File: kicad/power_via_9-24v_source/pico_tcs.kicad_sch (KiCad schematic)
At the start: 14 parts, among them J1 TCS/Power, J2 Conn_01x20_Male, J3 Conn_01x20_Male, J4 Keypad, J5 Display, U1 L7805, U2 ULN2003

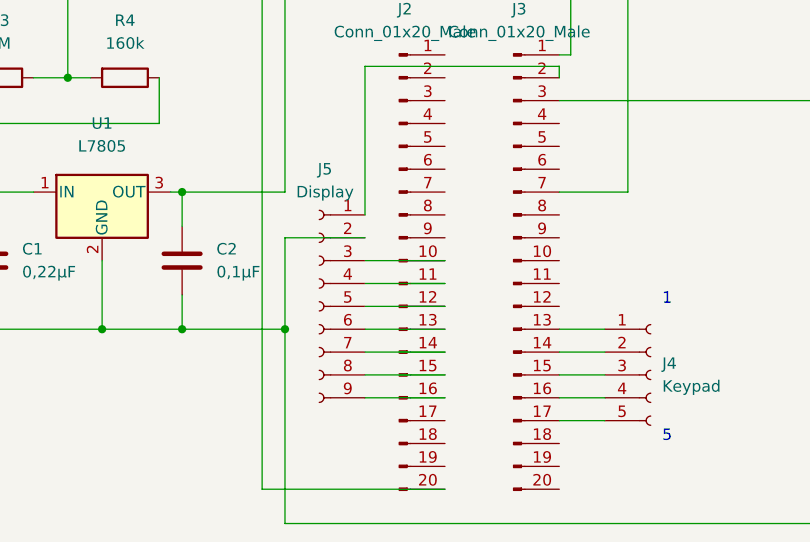
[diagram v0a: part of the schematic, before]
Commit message: fixed bug in connection between display and pico
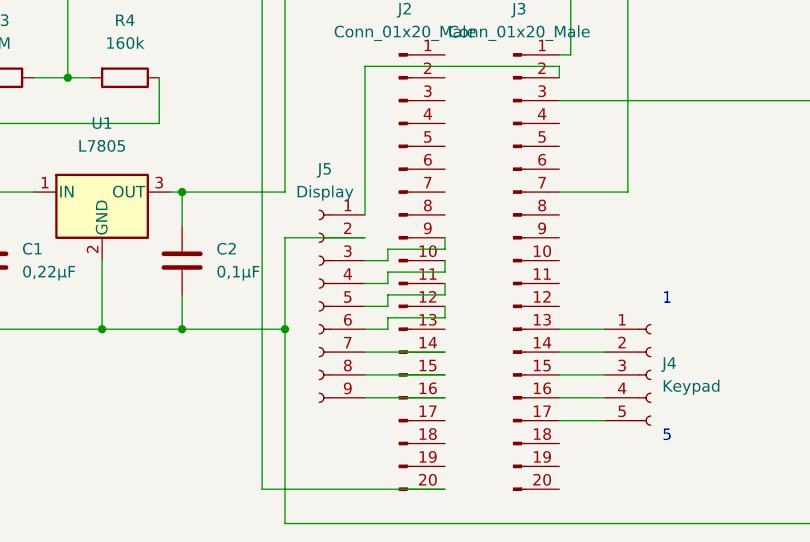
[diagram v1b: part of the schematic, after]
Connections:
- net at J5.3 (Pin_3): now also J2.9 (Pin_9); no longer J2.10 (Pin_10)
- net at J5.4 (Pin_4): now also J2.10 (Pin_10); no longer J2.11 (Pin_11)
- net at J5.5 (Pin_5): now also J2.11 (Pin_11); no longer J2.12 (Pin_12)
- net at J5.6 (Pin_6): now also J2.12 (Pin_12); no longer J2.13 (Pin_13)
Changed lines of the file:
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@@
+    (stroke (width 0) (type default) (color 0 0 0 0))
+  )
+  (wire (pts (xy 121.92 68.58) (xy 128.27 68.58))
     (stroke (width 0) (type default) (color 0 0 0 0))
   )
@@
     (stroke (width 0) (type default) (color 0 0 0 0))
   )
+  (wire (pts (xy 119.38 67.31) (xy 121.92 67.31))
+    (stroke (width 0) (type default) (color 0 0 0 0))
+  )
+  (wire (pts (xy 121.92 64.77) (xy 121.92 63.5))
+    (stroke (width 0) (type default) (color 0 0 0 0))
+  )
   (wire (pts (xy 119.38 59.69) (xy 110.49 59.69))
     (stroke (width 0) (type default) (color 0 0 0 0))
@@
     (stroke (width 0) (type default) (color 0 0 0 0))
   )
+  (wire (pts (xy 128.27 63.5) (xy 128.27 62.23))
+    (stroke (width 0) (type default) (color 0 0 0 0))
+  )
+  (wire (pts (xy 121.92 66.04) (xy 128.27 66.04))
+    (stroke (width 0) (type default) (color 0 0 0 0))
+  )
   (wire (pts (xy 110.49 69.85) (xy 99.06 69.85))
     (stroke (width 0) (type default) (color 0 0 0 0))
   )
-  (wire (pts (xy 119.38 69.85) (xy 128.27 69.85))
-    (stroke (width 0) (type default) (color 0 0 0 0))
-  )
   (wire (pts (xy 96.52 46.99) (xy 66.04 46.99))
     (stroke (width 0) (type default) (color 0 0 0 0))
@@
     (stroke (width 0) (type default) (color 0 0 0 0))
   )
+  (wire (pts (xy 121.92 60.96) (xy 128.27 60.96))
+    (stroke (width 0) (type default) (color 0 0 0 0))
+  )
   (wire (pts (xy 66.04 46.99) (xy 66.04 62.23))
     (stroke (width 0) (type default) (color 0 0 0 0))
@@
     (stroke (width 0) (type default) (color 0 0 0 0))
   )
+  (wire (pts (xy 121.92 62.23) (xy 121.92 60.96))
+    (stroke (width 0) (type default) (color 0 0 0 0))
+  )
+  (wire (pts (xy 128.27 68.58) (xy 128.27 67.31))
+    (stroke (width 0) (type default) (color 0 0 0 0))
+  )
+  (wire (pts (xy 121.92 67.31) (xy 121.92 66.04))
+    (stroke (width 0) (type default) (color 0 0 0 0))
+  )
   (wire (pts (xy 64.77 33.02) (xy 72.39 33.02))
     (stroke (width 0) (type default) (color 0 0 0 0))
@@
     (stroke (width 0) (type default) (color 0 0 0 0))
   )
-  (wire (pts (xy 119.38 62.23) (xy 128.27 62.23))
-    (stroke (width 0) (type default) (color 0 0 0 0))
-  )
   (wire (pts (xy 148.59 25.4) (xy 148.59 54.61))
     (stroke (width 0) (type default) (color 0 0 0 0))
@@
     (stroke (width 0) (type default) (color 0 0 0 0))
   )
+  (wire (pts (xy 119.38 64.77) (xy 121.92 64.77))
+    (stroke (width 0) (type default) (color 0 0 0 0))
+  )
   (wire (pts (xy 119.38 77.47) (xy 128.27 77.47))
     (stroke (width 0) (type default) (color 0 0 0 0))
@@
     (stroke (width 0) (type default) (color 0 0 0 0))
   )
-  (wire (pts (xy 119.38 64.77) (xy 128.27 64.77))
-    (stroke (width 0) (type default) (color 0 0 0 0))
-  )
   (wire (pts (xy 140.97 40.64) (xy 140.97 41.91))
     (stroke (width 0) (type default) (color 0 0 0 0))
@@
     (stroke (width 0) (type default) (color 0 0 0 0))
   )
+  (wire (pts (xy 119.38 62.23) (xy 121.92 62.23))
+    (stroke (width 0) (type default) (color 0 0 0 0))
+  )
   (wire (pts (xy 110.49 91.44) (xy 168.91 91.44))
     (stroke (width 0) (type default) (color 0 0 0 0))
@@
     (stroke (width 0) (type default) (color 0 0 0 0))
   )
-  (wire (pts (xy 119.38 67.31) (xy 128.27 67.31))
+  (wire (pts (xy 119.38 69.85) (xy 121.92 69.85))
     (stroke (width 0) (type default) (color 0 0 0 0))
   )
@@
     (stroke (width 0) (type default) (color 0 0 0 0))
   )
+  (wire (pts (xy 128.27 60.96) (xy 128.27 59.69))
+    (stroke (width 0) (type default) (color 0 0 0 0))
+  )
   (wire (pts (xy 16.51 24.13) (xy 16.51 20.32))
     (stroke (width 0) (type default) (color 0 0 0 0))
@@
     (stroke (width 0) (type default) (color 0 0 0 0))
   )
+  (wire (pts (xy 121.92 63.5) (xy 128.27 63.5))
+    (stroke (width 0) (type default) (color 0 0 0 0))
+  )
   (wire (pts (xy 140.97 80.01) (xy 146.05 80.01))
     (stroke (width 0) (type default) (color 0 0 0 0))
@@
     (stroke (width 0) (type default) (color 0 0 0 0))
   )
+  (wire (pts (xy 128.27 66.04) (xy 128.27 64.77))
+    (stroke (width 0) (type default) (color 0 0 0 0))
+  )
   (wire (pts (xy 77.47 54.61) (xy 77.47 58.42))
     (stroke (width 0) (type default) (color 0 0 0 0))
   )
+  (wire (pts (xy 121.92 69.85) (xy 121.92 68.58))
+    (stroke (width 0) (type default) (color 0 0 0 0))
+  )
